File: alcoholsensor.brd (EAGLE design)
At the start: 51.3 x 59.6 mm, 23 parts, among them IC2 7805TV

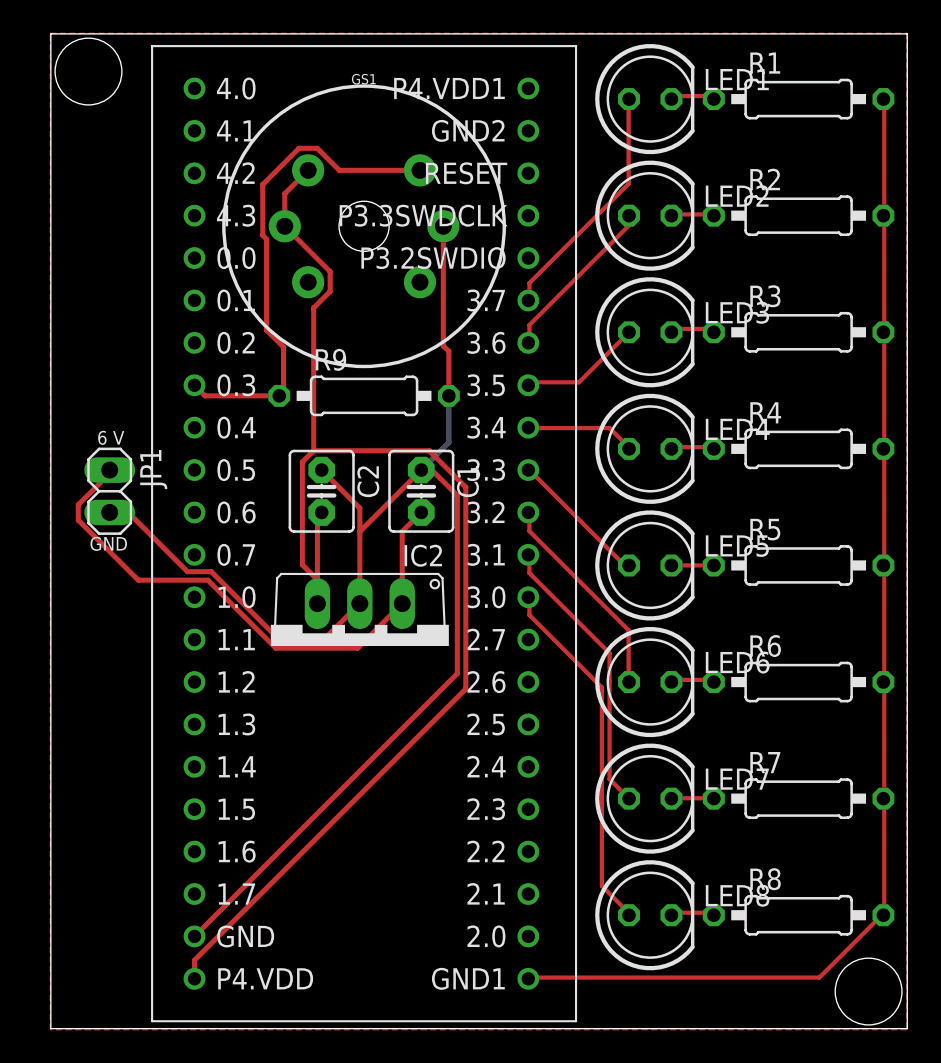
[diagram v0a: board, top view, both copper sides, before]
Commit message: Added pushbutton switch to control power source
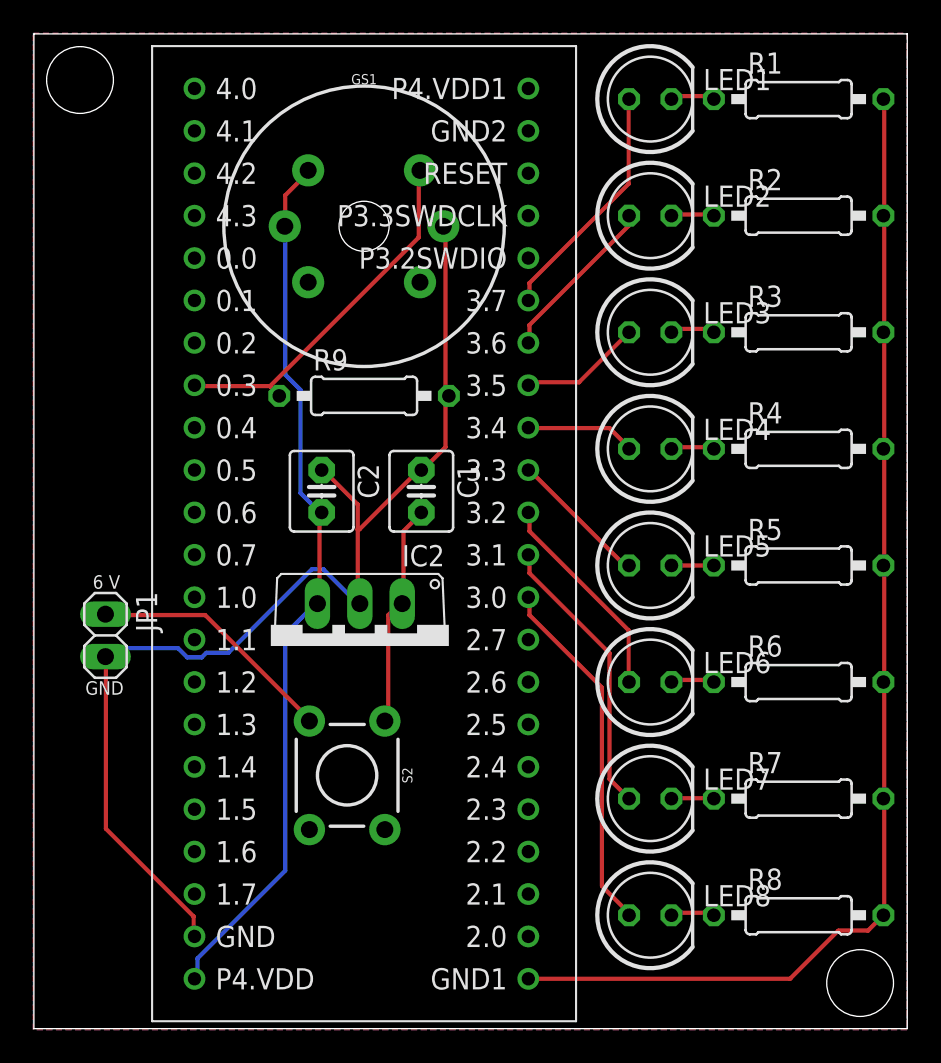
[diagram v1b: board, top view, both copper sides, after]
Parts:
- added S2: MOMENTARY-SWITCH-SPST-PTH-6.0MM, SparkFun-Switches:TACTILE_SWITCH_PTH_6.0MM
- moved JP1 8.64 mm to (34.0, 47.2)
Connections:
- net N$1 renamed RED
- net N$17 renamed GND2
- net N$2 renamed RED1
- net N$20 renamed 5V
- net N$21 renamed DATA
- net N$22 renamed GND1
- net N$3 renamed ORANGE
- net N$4 renamed ORANGE1
- net N$5 renamed GREEN
- net N$6 renamed GREEN1
- net N$7 renamed BLUE
- net N$8 renamed BLUE1
- removed net N$18: C1.2, IC2.1, JP1.1
- new net 6V: C1.2, IC2.1, S2.1
- new net N$1: JP1.1, S2.3
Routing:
- net N$18: track 33.4 -> 0.00 mm
- net 5V: track 80.5 -> 53.3 mm
- net GND1: track 84.3 -> 67.6 mm
- net N$1: track 0.00 -> 14.9 mm
- net 6V: track 0.00 -> 13.5 mm
- net DATA: track 29.5 -> 22.0 mm
- added copper zone on layer 1, net N$2
- added copper zone on layer 16, net N$3
- removed copper zone on layer 1, net N$19
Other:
- board size 51.3 x 59.6 mm -> 52.3 x 59.6 mm
